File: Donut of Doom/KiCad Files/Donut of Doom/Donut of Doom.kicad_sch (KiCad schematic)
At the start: 16 parts

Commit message: Made draft pcb for Plant Donut V2
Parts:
- added D4: LED, LED_SMD:LED_0603_1608Metric_Pad1.05x0.95mm_HandSolder, symbol Device:LED
- U1: footprint (none) -> adafruit_h3lis331:Adafruit_H3LIS331; symbol Battlebots Symbols:CJMCU-MPU -> adafruit_h3lis331:Adafruit_H3LIS331
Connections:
- net +3V3: now also U1.VIN (Vin); no longer U1. (GND)
- net GND: now also U1.GND, D4.1 (K); no longer U1. (GND)
- net GPIO4: now also D4.2 (A)
- net I2C0 SCL: now also U1.SCL; no longer U1. (GND)
- net I2C0 SDA: now also U1.SDA; no longer U1. (GND)
- new net: ESC1. (C), M1. (C/L1) (x2)
- new net: ESC2. (C), M2. (C/L1) (x2)
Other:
- note added: "Debug LED"
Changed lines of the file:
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@@
 	(text "Directional LED indicator (mutable)\n\n"
 		(exclude_from_sim no)
-		(at 44.196 203.708 0)
+		(at 45.466 193.294 0)
 		(effects
 			(font
@@
 		)
 	)
+	(text "Debug LED"
+		(exclude_from_sim no)
+		(at 61.976 212.09 0)
+		(effects
+			(font
+				(size 1.27 1.27)
+			)
+		)
+	)
 	(text "Pico 2 has a 5v to 3V3 regulator\n"
 		(exclude_from_sim no)
@@
 	)
 	(junction
+		(at 44.45 208.28)
+		(diameter 0)
+		(color 0 0 0 0)
+	)
+	(junction
+		(at 44.45 222.25)
+		(diameter 0)
+		(color 0 0 0 0)
+	)
+	(junction
 		(at 168.91 76.2)
 		(diameter 0)
@@
 	(wire
 		(pts
-			(xy 181.61 76.2) (xy 199.39 76.2)
+			(xy 44.45 208.28) (xy 44.45 210.82)
 		)
 		(stroke
@@
 	(wire
 		(pts
-			(xy 66.04 137.16) (xy 66.04 138.43)
+			(xy 181.61 76.2) (xy 199.39 76.2)
 		)
 		(stroke
@@
 	(wire
 		(pts
+			(xy 54.61 218.44) (xy 54.61 222.25)
+		)
+		(stroke
+			(width 0)
+			(type default)
+		)
+	)
+	(wire
+		(pts
 			(xy 217.17 38.1) (xy 226.06 38.1)
 		)
@@
 	(wire
 		(pts
-			(xy 44.45 222.25) (xy 44.45 218.44)
+			(xy 44.45 226.06) (xy 44.45 222.25)
 		)
 		(stroke
@@
 	(wire
 		(pts
-			(xy 44.45 209.55) (xy 44.45 210.82)
+			(xy 44.45 201.93) (xy 44.45 208.28)
 		)
 		(stroke
@@
 	(wire
 		(pts
-			(xy 69.85 142.24) (xy 66.04 142.24)
+			(xy 54.61 210.82) (xy 54.61 208.28)
 		)
 		(stroke
@@
 	(wire
 		(pts
-			(xy 69.85 146.05) (xy 66.04 146.05)
+			(xy 217.17 69.85) (xy 218.44 69.85)
 		)
 		(stroke
@@
 	(wire
 		(pts
-			(xy 217.17 69.85) (xy 218.44 69.85)
+			(xy 195.58 85.09) (xy 195.58 88.9)
 		)
 		(stroke
@@
 	(wire
 		(pts
-			(xy 195.58 85.09) (xy 195.58 88.9)
+			(xy 163.83 43.18) (xy 168.91 43.18)
 		)
 		(stroke
@@
 	(wire
 		(pts
-			(xy 163.83 43.18) (xy 168.91 43.18)
+			(xy 66.04 142.24) (xy 72.39 142.24)
 		)
 		(stroke
@@
 	(wire
 		(pts
+			(xy 54.61 222.25) (xy 44.45 222.25)
+		)
+		(stroke
+			(width 0)
+			(type default)
+		)
+	)
+	(wire
+		(pts
 			(xy 218.44 76.2) (xy 226.06 76.2)
 		)
@@
 	(wire
 		(pts
+			(xy 44.45 222.25) (xy 44.45 218.44)
+		)
+		(stroke
+			(width 0)
+			(type default)
+		)
+	)
+	(wire
+		(pts
+			(xy 66.04 146.05) (xy 72.39 146.05)
+		)
+		(stroke
+			(width 0)
+			(type default)
+		)
+	)
+	(wire
+		(pts
 			(xy 177.8 201.93) (xy 180.34 201.93)
 		)
@@
 	(wire
 		(pts
+			(xy 54.61 208.28) (xy 44.45 208.28)
+		)
+		(stroke
+			(width 0)
+			(type default)
+		)
+	)
+	(wire
+		(pts
 			(xy 185.42 46.99) (xy 185.42 53.34)
 		)
@@
 	(wire
 		(pts
-			(xy 66.04 137.16) (xy 68.58 137.16)
+			(xy 66.04 138.43) (xy 68.58 138.43)
 		)
 		(stroke
@@
 		)
 	)
+	(wire
+		(pts
+			(xy 68.58 138.43) (xy 68.58 137.16)
+		)
+		(stroke
+			(width 0)
+			(type default)
+		)
+	)
 	(image
 		(at 227.33 227.33)
@@
 	)
 	(label "I2C0 SCL"
-		(at 69.85 142.24 0)
+		(at 72.39 146.05 0)
 		(effects
 			(font
@@
 	)
 	(label "I2C0 SDA"
-		(at 69.85 146.05 0)
+		(at 72.39 142.24 0)
 		(effects
 			(font
@@
 	)
 	(label "GPIO4"
-		(at 44.45 209.55 180)
+		(at 44.45 201.93 180)
 		(effects
 			(font
@@
 	)
 	(symbol
+		(lib_id "Device:LED")
+		(at 54.61 214.63 90)
+		(unit 1)
+		(exclude_from_sim no)
+		(in_bom yes)
+		(on_board yes)
+		(dnp no)
+		(fields_autoplaced yes)
+		(property "Reference" "D4"
+			(at 58.42 214.9474 90)
+			(effects
+				(font
+					(size 1.27 1.27)
+				)
+				(justify right)
+			)
+		)
+		(property "Value" "LED"
+			(at 58.42 217.4874 90)
+			(effects
+				(font
+					(size 1.27 1.27)
+				)
+				(justify right)
+			)
+		)
+		(property "Footprint" "LED_SMD:LED_0603_1608Metric_Pad1.05x0.95mm_HandSolder"
+			(at 54.61 214.63 0)
+			(effects
+				(font
+					(size 1.27 1.27)
+				)
+				(hide yes)
+			)
+		)
+		(property "Datasheet" "~"
+			(at 54.61 214.63 0)
+			(effects
+				(font
+					(size 1.27 1.27)
+				)
+				(hide yes)
+			)
+		)
+		(property "Description" "Light emitting diode"
+			(at 54.61 214.63 0)
+			(effects
+				(font
+					(size 1.27 1.27)
+				)
+				(hide yes)
+			)
+		)
+		(property "Sim.Pins" "1=K 2=A"
+			(at 54.61 214.63 0)
+			(effects
+				(font
+					(size 1.27 1.27)
+				)
+				(hide yes)
+			)
+		)
+		(pin "1"
+		)
+		(pin "2"
+		)
+		(instances
+			(project "Donut of Doom"
+				(path "/f9c3bb91-9ef9-468e-b931-f1acff0425cb"
+					(reference "D4")
+					(unit 1)
+				)
+			)
+		)
+	)
+	(symbol
 		(lib_id "power:+BATT")
 		(at 195.58 35.56 0)
@@
 	(symbol
 		(lib_id "power:GND")
-		(at 44.45 222.25 0)
+		(at 44.45 226.06 0)
 		(unit 1)
 		(exclude_from_sim no)
@@
 		(dnp no)
 		(property "Reference" "#PWR013"
-			(at 44.45 228.6 0)
+			(at 44.45 232.41 0)
 			(effects
 				(font
@@
 		)
 		(property "Value" "GND"
-			(at 47.752 223.012 0)
+			(at 47.752 226.822 0)
 			(effects
 				(font
@@
 		)
 		(property "Footprint" ""
-			(at 44.45 222.25 0)
+			(at 44.45 226.06 0)
 			(effects
 				(font
@@
 		)
 		(property "Datasheet" ""
-			(at 44.45 222.25 0)
+			(at 44.45 226.06 0)
 			(effects
 				(font
@@
 		)
 		(property "Description" "Power symbol creates a global label with name \"GND\" , ground"
-			(at 44.45 222.25 0)
+			(at 44.45 226.06 0)
 			(effects
 				(font
@@
 	)
 	(symbol
-		(lib_id "Battlebots Symbols:CJMCU-MPU")
-		(at 50.8 156.21 0)
-		(mirror y)
+		(lib_id "adafruit_h3lis331:Adafruit_H3LIS331")
+		(at 52.07 154.94 0)
 		(unit 1)
 		(exclude_from_sim no)
@@
 		(dnp no)
 		(property "Reference" "U1"
-			(at 34.544 171.958 0)
+			(at 68.326 170.688 0)
 			(effects
 				(font
@@
 		)
 		(property "Value" "~"
-			(at 34.544 174.498 0)
+			(at 68.326 173.228 0)
 			(effects
 				(font
@@
 			)
 		)
-		(property "Footprint" ""
-			(at 50.8 156.21 0)
+		(property "Footprint" "adafruit_h3lis331:Adafruit_H3LIS331"
+			(at 52.07 154.94 0)
 			(effects
 				(font
@@
 		)
 		(property "Datasheet" ""
-			(at 50.8 156.21 0)
+			(at 52.07 154.94 0)
 			(effects
 				(font
@@
 		)
 		(property "Description" ""
-			(at 50.8 156.21 0)
+			(at 52.07 154.94 0)
 			(effects
 				(font
@@
 			)
 		)
-		(pin ""
+		(pin "CS"
 		)
-		(pin ""
+		(pin "SDA"
 		)
-		(pin ""
+		(pin "NC"
 		)
-		(pin ""
+		(pin "SCL"
 		)
-		(pin ""
+		(pin "GND"
 		)
-		(pin ""
+		(pin "VIN"
 		)
-		(pin ""
+		(pin "SDO"
 		)
-		(pin ""
+		(pin "INT"
 		)
-		(pin ""
+		(pin "3V"
 		)
-		(pin ""
+		(pin "I2"
 		)
 		(instances

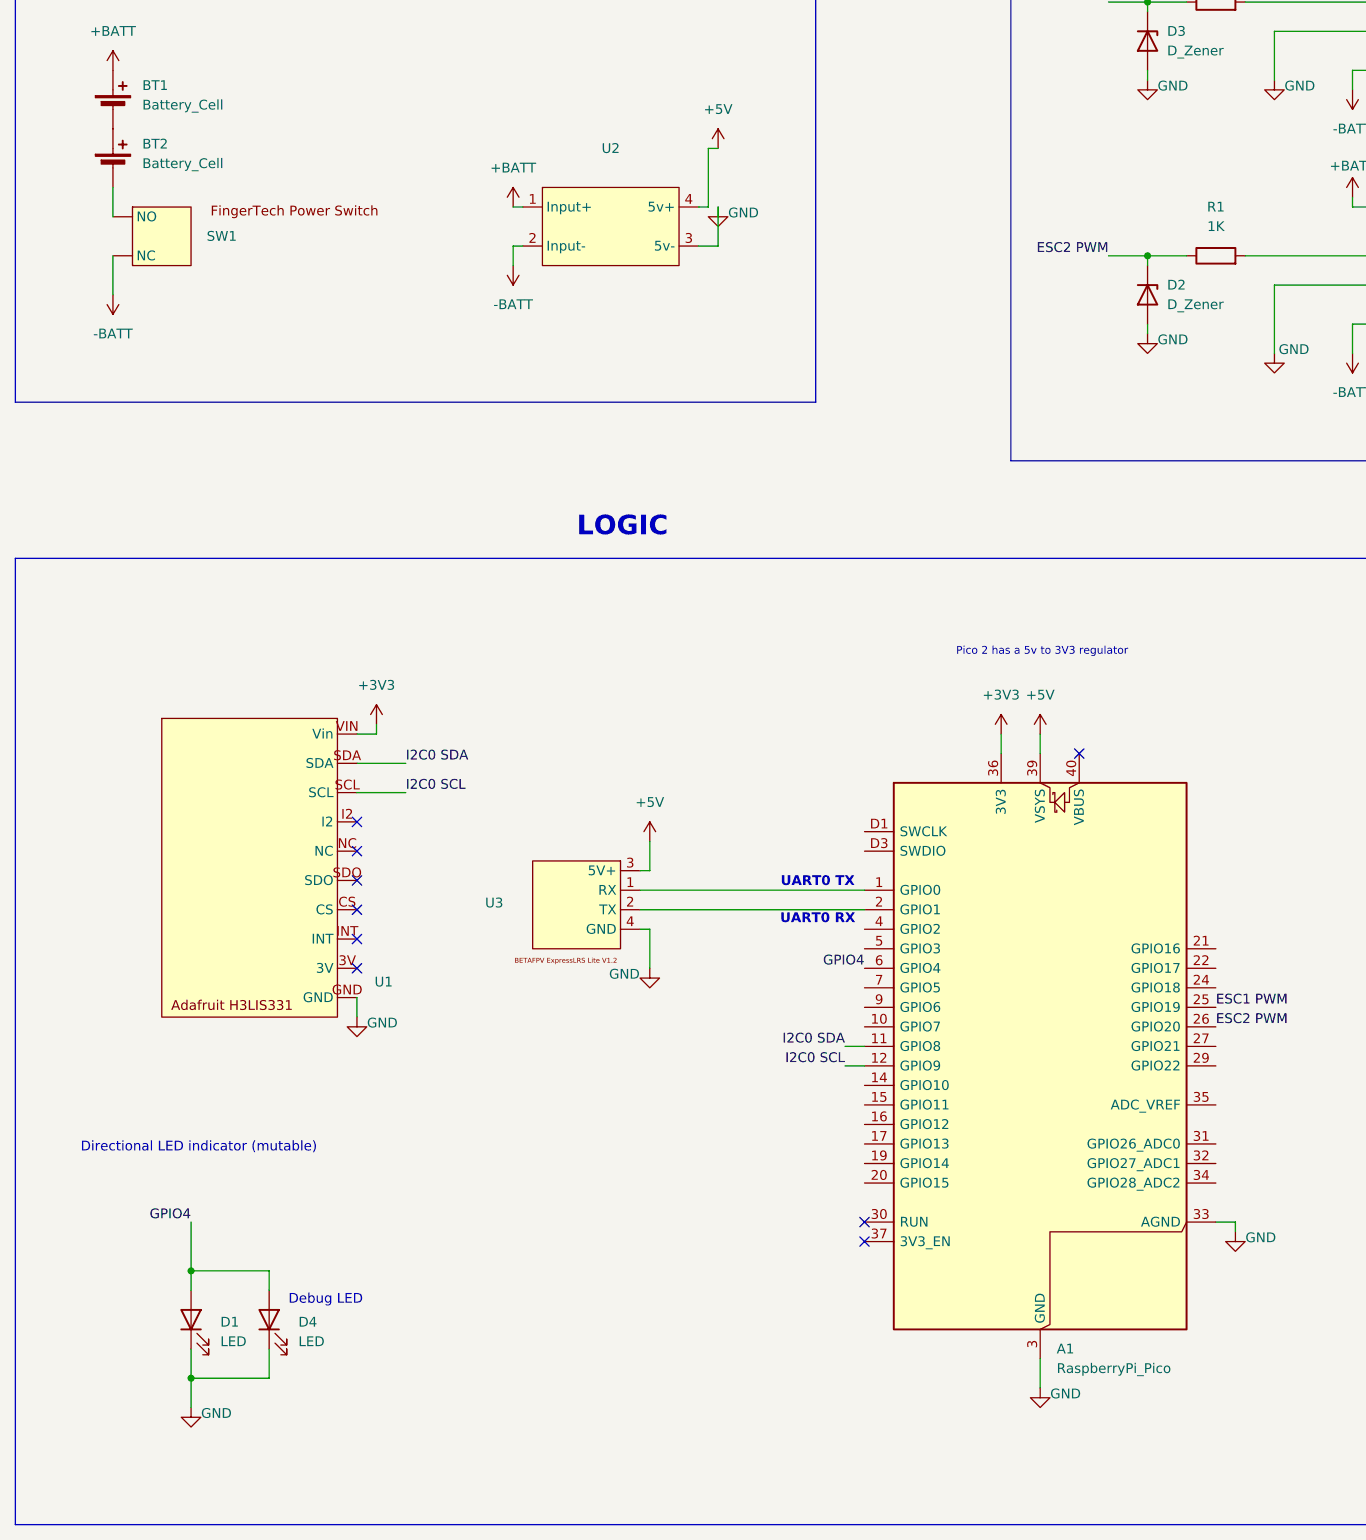
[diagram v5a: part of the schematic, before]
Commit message: debug resistor and led finalized, export tested for dfm
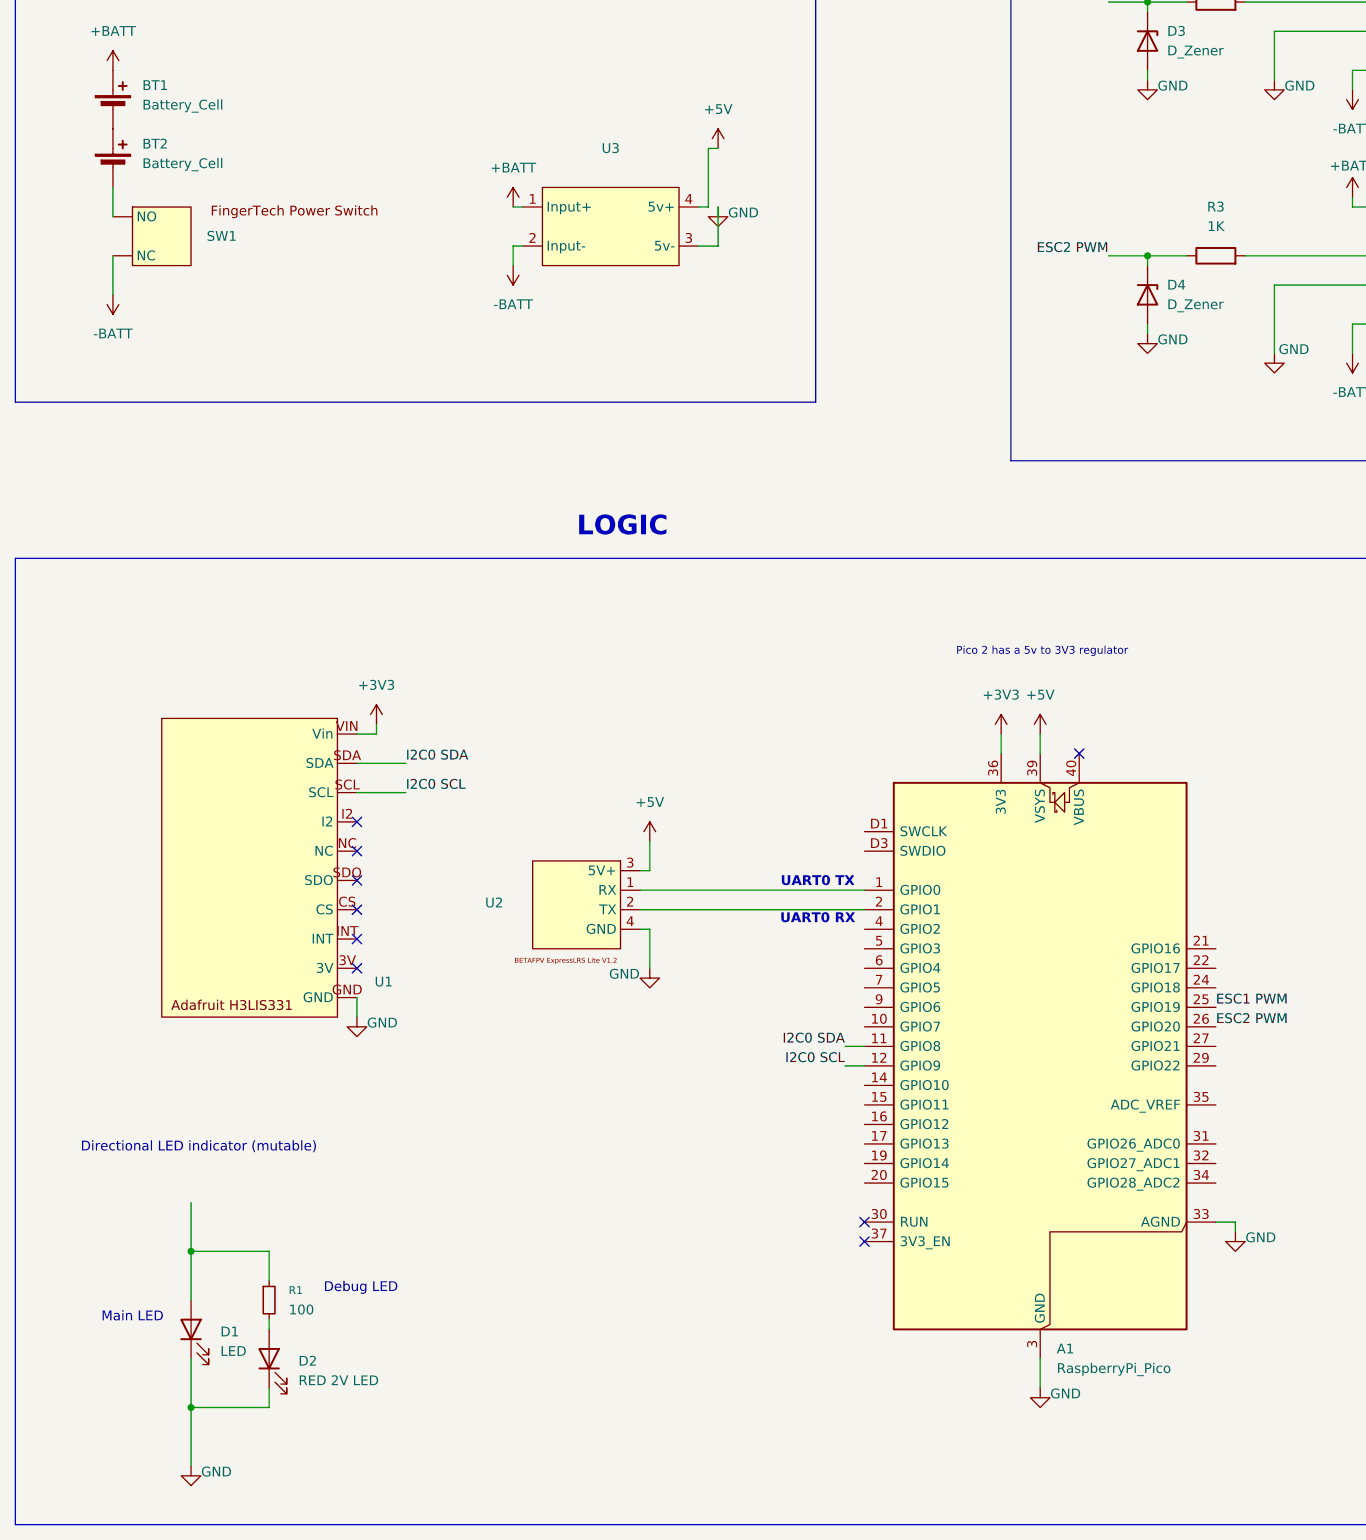
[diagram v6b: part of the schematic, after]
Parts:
- added R1: 100, Resistor_SMD:R_0603_1608Metric_Pad0.98x0.95mm_HandSolder, symbol Device:R_Small
- D2: renamed from D4; value LED -> RED 2V LED
- renumbered D2 to D4, R1 to R3, U3 to U2, U2 to U3
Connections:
- removed net GPIO4: A1.6 (GPIO4), D1.2 (A), D2.2 (A)
- new net: ESC1. (C), M1. (C/L1) (x2)
- new net: D1.2 (A), R1.1
- new net: D2.2 (A), R1.2
- new net: ESC2. (C), M2. (C/L1) (x2)
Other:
- note added: "Main LED"
- moved on the sheet: D1, D2
